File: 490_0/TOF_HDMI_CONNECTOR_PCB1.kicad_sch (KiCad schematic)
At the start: 4 parts, among them J12 2000-1-1-20-00-BK

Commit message: LED names + 5V routing through ESD + renamed ESD chips to "U"
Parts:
- renumbered CR7 to U12
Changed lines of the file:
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@@
 		(dnp no)
 		(fields_autoplaced yes)
-		(property "Reference" "CR7"
+		(property "Reference" "U12"
 			(at 170.18 96.52 0)
 			(effects
@@
 			(project "490_0"
 				(path "/365a82ed-827d-43e1-aa2f-b98221c4179c/f9f22bb2-829e-4ff5-89be-c4b5e2122135/a0c8e7b0-f2bd-4dbc-92d9-c214cdc6de2b"
-					(reference "CR7")
+					(reference "U12")
 					(unit 1)
 				)

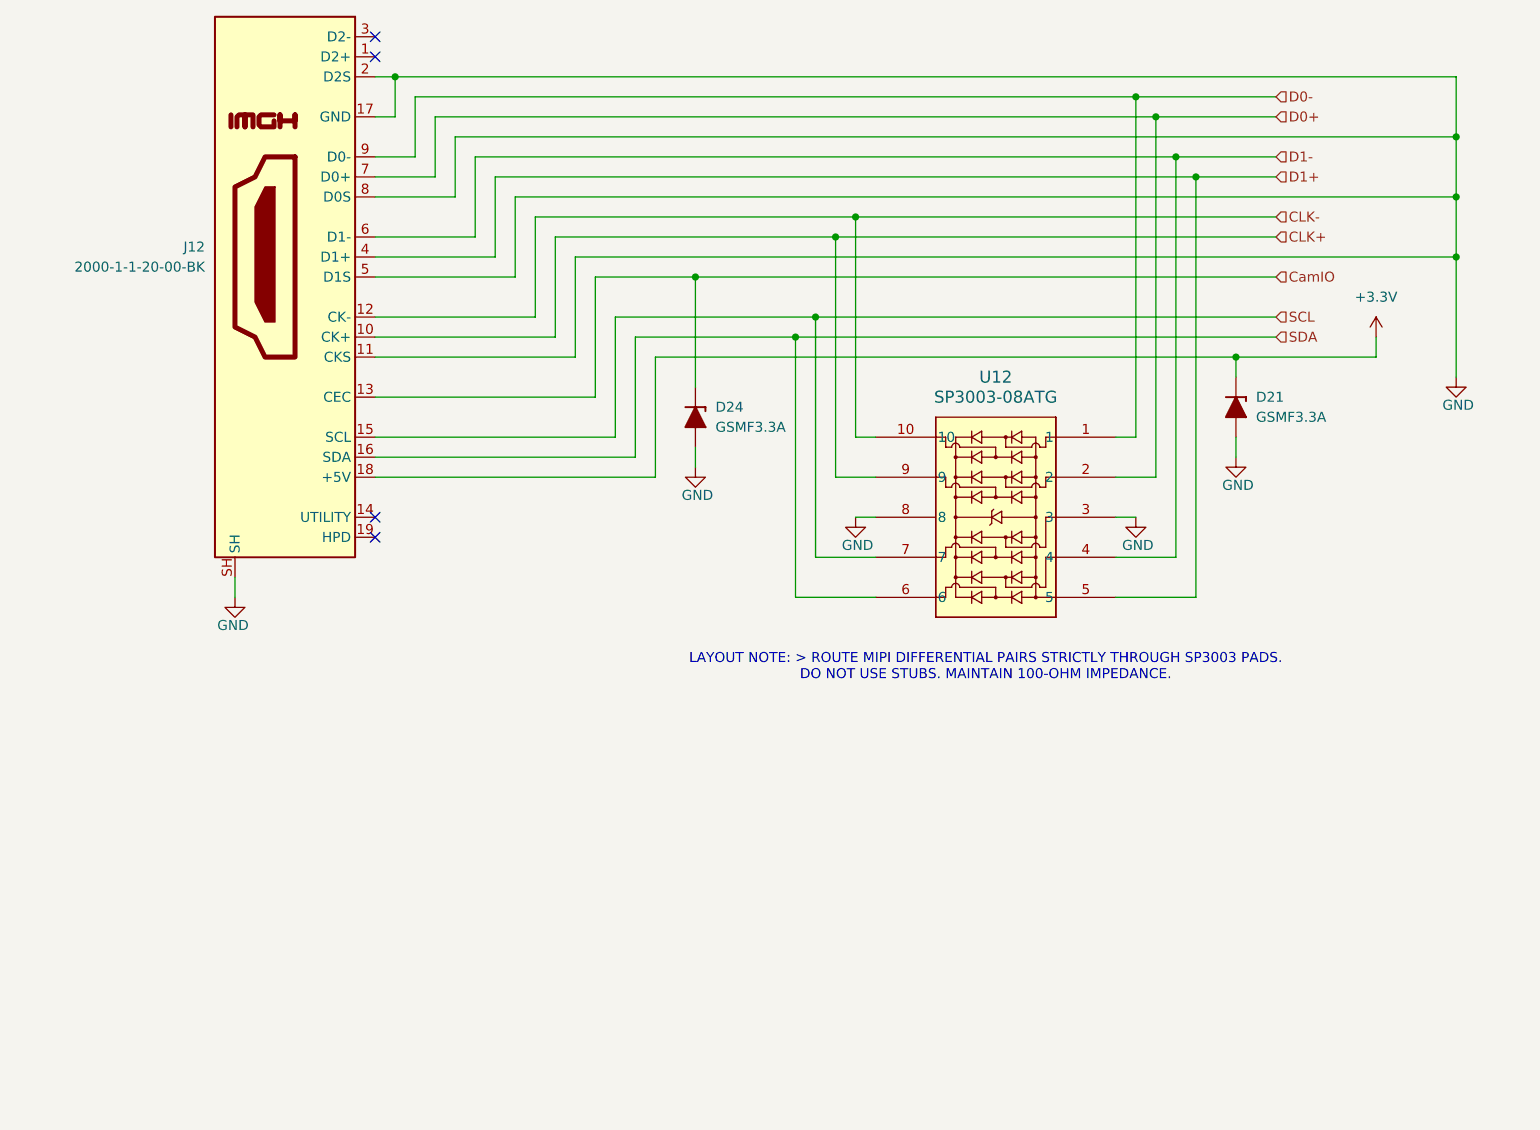
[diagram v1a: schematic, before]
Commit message: Changed ESD chip for HDMI
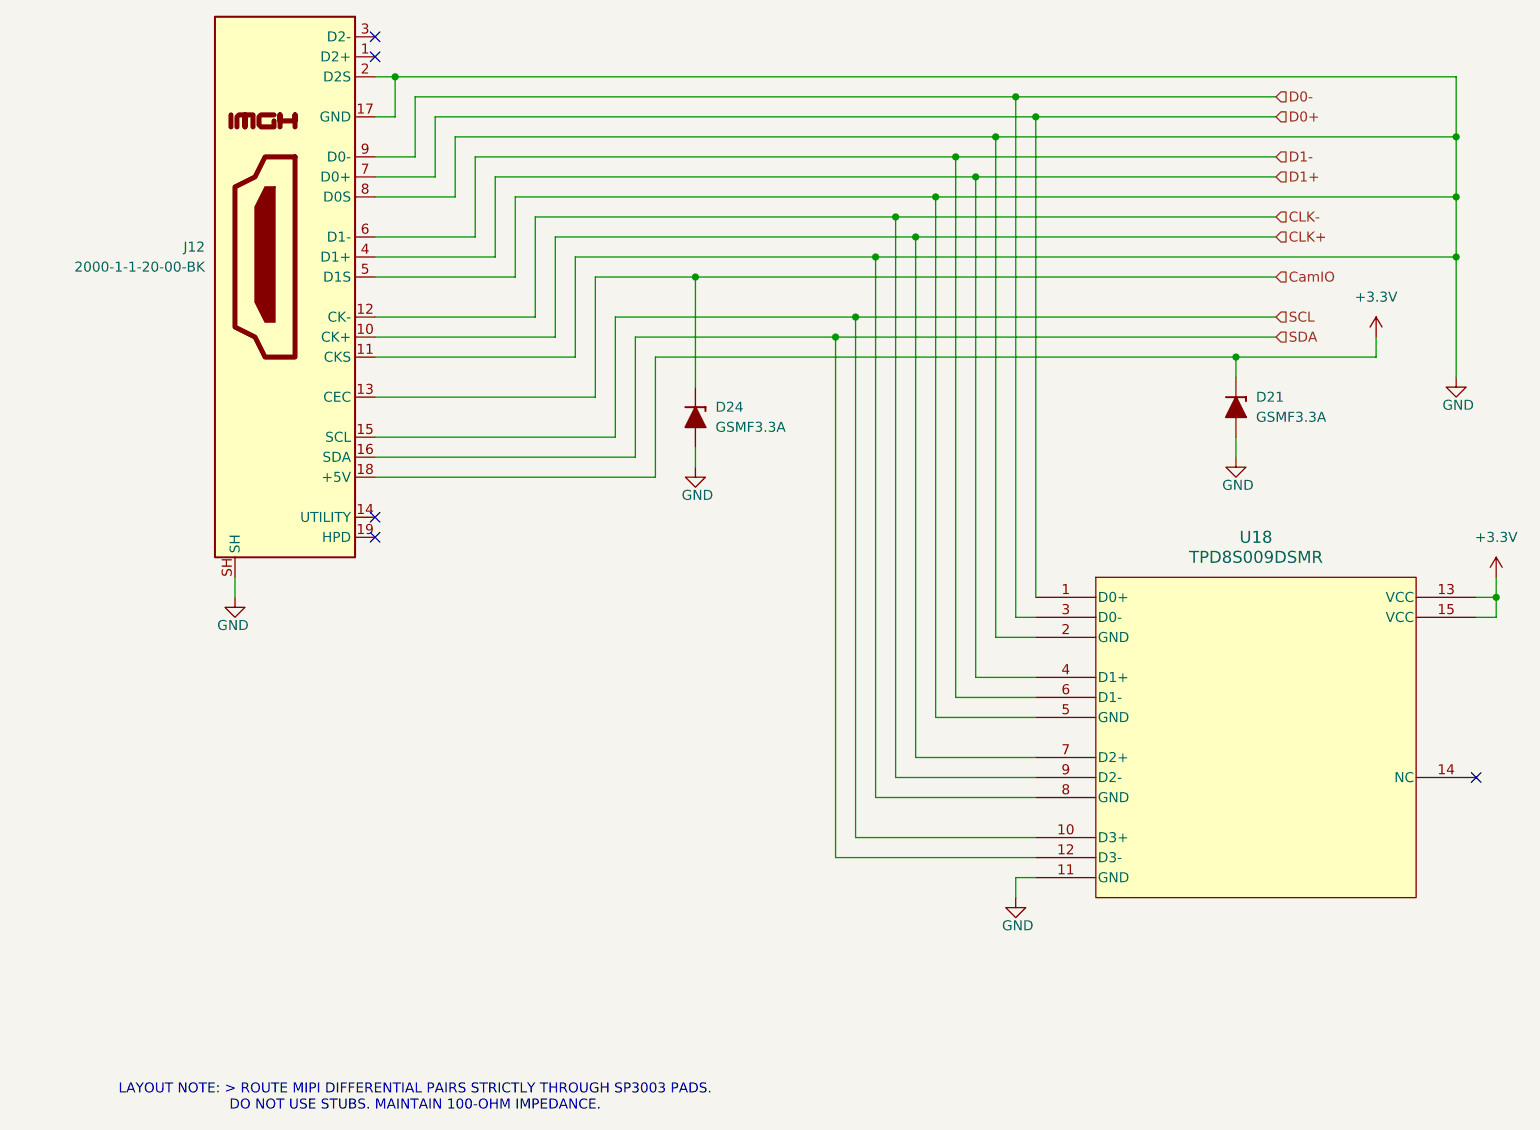
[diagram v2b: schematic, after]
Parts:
- removed U12: SP3003-08ATG, *CapStone*:MSOP10_MO-187_LTF, symbol capstone_parts:SP3003-08ATG
- added U18: TPD8S009DSMR, *CapStone*:TPD8S009DSMR, symbol capstone_parts:TPD8S009DSMR
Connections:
- net +3.3V: now also U18.13 (VCC), U18.15 (VCC)
- net CLK+: now also U18.7 (D2+)
- net CLK-: now also U18.9 (D2-)
- net D0+: now also U18.1 (D0+)
- net D0-: now also U18.3 (D0-)
- net D1+: now also U18.4 (D1+)
- net D1-: now also U18.6 (D1-)
- net GND: now also U18.11 (GND), U18.2 (GND), U18.5 (GND), U18.8 (GND)
- net SCL: now also U18.10 (D3+)
- net SDA: now also U18.12 (D3-)
- no-connect marks 4 -> 5

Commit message: PCB Jumpstart
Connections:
- net GND: now also J12.SH1, J12.SH2, J12.SH3, J12.SH4; no longer J12.SH
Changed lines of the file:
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@@
+	)
+	(junction
+		(at 74.93 127)
+		(diameter 0)
+		(color 0 0 0 0)
 	)
 	(junction
@@
 	)
 	(junction
+		(at 77.47 127)
+		(diameter 0)
+		(color 0 0 0 0)
+	)
+	(junction
 		(at 149.86 91.44)
 		(diameter 0)
@@
 	)
 	(junction
+		(at 76.2 127)
+		(diameter 0)
+		(color 0 0 0 0)
+	)
+	(junction
 		(at 228.6 66.04)
 		(diameter 0)
@@
 	(wire
 		(pts
+			(xy 72.39 124.46) (xy 72.39 127)
+		)
+		(stroke
+			(width 0)
+			(type default)
+		)
+	)
+	(wire
+		(pts
 			(xy 119.38 83.82) (xy 119.38 99.06)
 		)
@@
 	(wire
 		(pts
+			(xy 74.93 124.46) (xy 74.93 127)
+		)
+		(stroke
+			(width 0)
+			(type default)
+		)
+	)
+	(wire
+		(pts
 			(xy 96.52 68.58) (xy 91.44 68.58)
 		)
@@
 	(wire
 		(pts
+			(xy 72.39 127) (xy 74.93 127)
+		)
+		(stroke
+			(width 0)
+			(type default)
+		)
+	)
+	(wire
+		(pts
 			(xy 228.6 73.66) (xy 228.6 81.28)
 		)
@@
 	(wire
 		(pts
-			(xy 73.66 124.46) (xy 73.66 121.92)
-		)
-		(stroke
-			(width 0)
-			(type default)
-		)
-	)
-	(wire
-		(pts
 			(xy 116.84 81.28) (xy 116.84 93.98)
 		)
@@
 	(wire
 		(pts
+			(xy 74.93 127) (xy 76.2 127)
+		)
+		(stroke
+			(width 0)
+			(type default)
+		)
+	)
+	(wire
+		(pts
 			(xy 170.18 129.54) (xy 170.18 66.04)
 		)
@@
 	(wire
 		(pts
+			(xy 77.47 124.46) (xy 77.47 127)
+		)
+		(stroke
+			(width 0)
+			(type default)
+		)
+	)
+	(wire
+		(pts
 			(xy 109.22 73.66) (xy 109.22 83.82)
 		)
@@
 	(wire
 		(pts
+			(xy 76.2 127) (xy 76.2 128.27)
+		)
+		(stroke
+			(width 0)
+			(type default)
+		)
+	)
+	(wire
+		(pts
+			(xy 80.01 124.46) (xy 80.01 127)
+		)
+		(stroke
+			(width 0)
+			(type default)
+		)
+	)
+	(wire
+		(pts
 			(xy 165.1 137.16) (xy 165.1 68.58)
 		)
@@
 	(wire
 		(pts
+			(xy 77.47 127) (xy 76.2 127)
+		)
+		(stroke
+			(width 0)
+			(type default)
+		)
+	)
+	(wire
+		(pts
 			(xy 165.1 68.58) (xy 205.74 68.58)
 		)
@@
 		(pts
 			(xy 175.26 63.5) (xy 175.26 124.46)
+		)
+		(stroke
+			(width 0)
+			(type default)
+		)
+	)
+	(wire
+		(pts
+			(xy 80.01 127) (xy 77.47 127)
 		)
 		(stroke
@@
 		(pin "8"
 		)
-		(pin "SH"
+		(pin "SH1"
+		)
+		(pin "SH2"
+		)
+		(pin "SH3"
+		)
+		(pin "SH4"
 		)
 		(instances
@@
 	(symbol
 		(lib_id "power:GND")
-		(at 73.66 124.46 0)
+		(at 76.2 128.27 0)
 		(unit 1)
 		(exclude_from_sim no)
@@
 		(dnp no)
 		(property "Reference" "#PWR0148"
-			(at 73.66 130.81 0)
+			(at 76.2 134.62 0)
 			(effects
 				(font
@@
 		)
 		(property "Value" "GND"
-			(at 73.406 128.016 0)
+			(at 75.946 131.826 0)
 			(effects
 				(font
@@
 		)
 		(property "Footprint" ""
-			(at 73.66 124.46 0)
+			(at 76.2 128.27 0)
 			(effects
 				(font
@@
 		)
 		(property "Datasheet" ""
-			(at 73.66 124.46 0)
+			(at 76.2 128.27 0)
 			(effects
 				(font
@@
 		)
 		(property "Description" "Power symbol creates a global label with name \"GND\" , ground"
-			(at 73.66 124.46 0)
-			(effects
-				(font
+			(at 76.2 128.27 0)
+			(effects
+				(font

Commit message: Added side B for SW1
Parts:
- D21, D24: symbol PCM_Diode_TVS_AKL:SMF5.0A -> capstone_parts:SMF5.0A
- J12: symbol Connector:HDMI_A -> capstone_parts:HDMI_A
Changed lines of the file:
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@@
 	)
 	(symbol
-		(lib_id "Connector:HDMI_A")
+		(lib_id "capstone_parts:HDMI_A")
 		(at 81.28 81.28 0)
 		(mirror y)
@@
 	)
 	(symbol
-		(lib_id "PCM_Diode_TVS_AKL:SMF5.0A")
+		(lib_id "capstone_parts:SMF5.0A")
 		(at 132.08 101.6 270)
 		(mirror x)
@@
 	)
 	(symbol
-		(lib_id "PCM_Diode_TVS_AKL:SMF5.0A")
+		(lib_id "capstone_parts:SMF5.0A")
 		(at 200.66 100.33 270)
 		(mirror x)

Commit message: Rerouted + external coponents update
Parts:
- removed D21: GSMF3.3A, Diode_SMD:D_SOD-123F, symbol capstone_parts:SMF5.0A
- added U19: SP3003-02XTG, *CapStone*:SOT553_LTF_SP3003_02XTG, symbol capstone_parts:SP3003-02XTG
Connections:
- net +3.3V: now also U19.3
- net GND: now also U19.2
- net SCL: now also U19.5; no longer U18.10 (D3+)
- net SDA: now also U19.4; no longer U18.12 (D3-)
- net USBhub_P: now reaches J12.1 (D2+)
- net USBhub_P: now also U18.10 (D3+)
- net USBhub_N: now reaches J12.3 (D2-)
- net USBhub_N: now also U18.12 (D3-)
- no-connect marks 5 -> 4

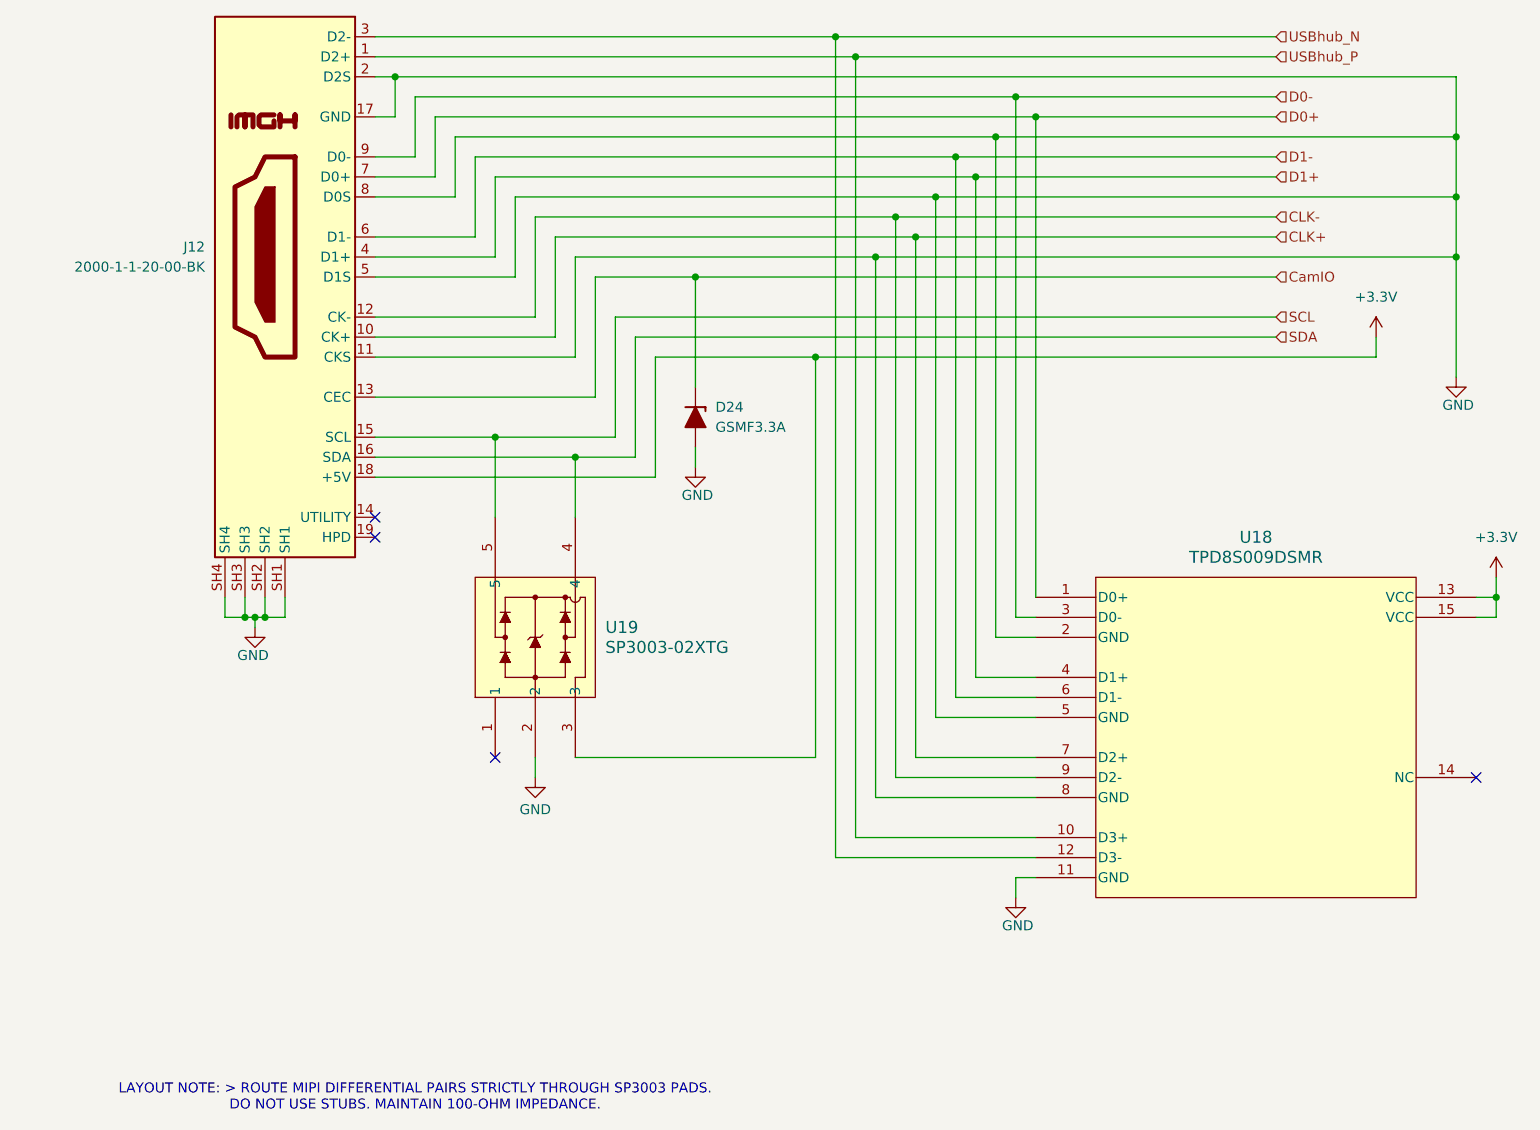
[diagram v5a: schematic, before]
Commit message: started routing up to HDMI ESD impedance matching
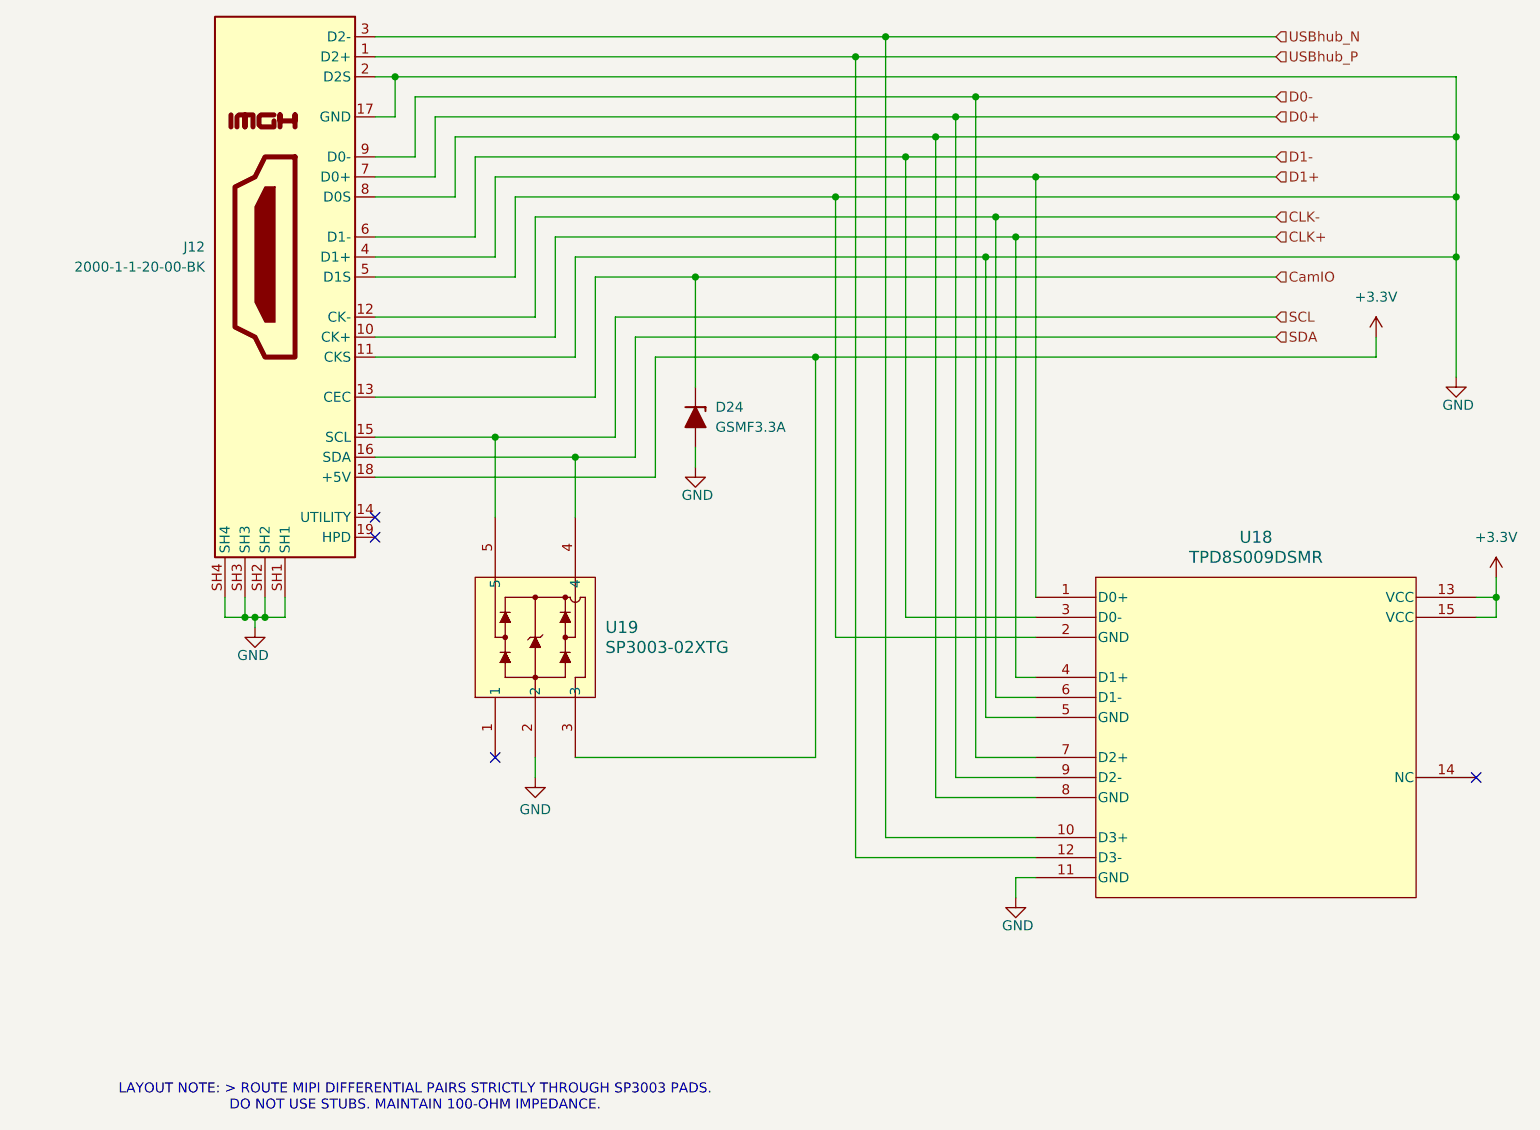
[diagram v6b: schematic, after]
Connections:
- net CLK+: now also U18.4 (D1+); no longer U18.7 (D2+)
- net CLK-: now also U18.6 (D1-); no longer U18.9 (D2-)
- net D0+: now also U18.9 (D2-); no longer U18.1 (D0+)
- net D0-: now also U18.7 (D2+); no longer U18.3 (D0-)
- net D1+: now also U18.1 (D0+); no longer U18.4 (D1+)
- net D1-: now also U18.3 (D0-); no longer U18.6 (D1-)
- net USBhub_N: now also U18.10 (D3+); no longer U18.12 (D3-)
- net USBhub_P: now also U18.12 (D3-); no longer U18.10 (D3+)

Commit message: Finished PCB1 routing
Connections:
- net CLK+: now also U18.12 (D3-); no longer U18.4 (D1+)
- net CLK-: now also U18.10 (D3+); no longer U18.6 (D1-)
- net D0+: now also J12.1 (D2+), U18.6 (D1-); no longer J12.7 (D0+), U18.9 (D2-)
- net D0-: now also J12.3 (D2-), U18.4 (D1+); no longer J12.9 (D0-), U18.7 (D2+)
- net D1+: now also U18.9 (D2-); no longer U18.1 (D0+)
- net D1-: now also U18.7 (D2+); no longer U18.3 (D0-)
- net USBhub_N: now also J12.9 (D0-), U18.1 (D0+); no longer J12.3 (D2-), U18.10 (D3+)
- net USBhub_P: now also J12.7 (D0+), U18.3 (D0-); no longer J12.1 (D2+), U18.12 (D3-)

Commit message: Friday, March 20th: PCB Final for BOM
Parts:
- J12: footprint *CapStone*:CNCTECH_2000-1-1-20-00-BK -> capstone:CNCTECH_2000-1-1-20-00-BK
- U18: footprint *CapStone*:TPD8S009DSMR -> capstone:TPD8S009DSMR
- U19: footprint *CapStone*:SOT553_LTF_SP3003_02XTG -> capstone:SOT553_LTF_SP3003_02XTG
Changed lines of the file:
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@@
 			)
 		)
-		(property "Footprint" "*CapStone*:CNCTECH_2000-1-1-20-00-BK"
+		(property "Footprint" "capstone:CNCTECH_2000-1-1-20-00-BK"
 			(at 80.645 81.28 0)
 			(effects
@@
 		)
 		(property "Unit" "pcs"
+			(at 81.28 81.28 0)
+			(effects
+				(font
+					(size 1.27 1.27)
+				)
+				(hide yes)
+			)
+		)
+		(property "OPTION" ""
 			(at 81.28 81.28 0)
 			(effects
@@
 			)
 		)
-		(property "Footprint" "*CapStone*:TPD8S009DSMR"
+		(property "Footprint" "capstone:TPD8S009DSMR"
 			(at 175.26 127 0)
 			(effects
@@
 		)
 		(property "Unit" "pcs"
+			(at 175.26 127 0)
+			(effects
+				(font
+					(size 1.27 1.27)
+				)
+				(hide yes)
+			)
+		)
+		(property "OPTION" ""
 			(at 175.26 127 0)
 			(effects
@@
 		)
 		(property "Unit" "pcs"
+			(at 132.08 101.6 90)
+			(effects
+				(font
+					(size 1.27 1.27)
+				)
+				(hide yes)
+			)
+		)
+		(property "OPTION" ""
 			(at 132.08 101.6 90)
 			(effects
@@
 			)
 		)
-		(property "Footprint" "*CapStone*:SOT553_LTF_SP3003_02XTG"
+		(property "Footprint" "capstone:SOT553_LTF_SP3003_02XTG"
 			(at 106.68 144.78 0)
 			(effects
@@
 			(at 106.68 144.78 90)
 			(effects
+				(font
+					(size 1.27 1.27)
+				)
+				(hide yes)
+			)
+		)
+		(property "OPTION" ""
+			(at 106.68 144.78 90)
+			(effects
